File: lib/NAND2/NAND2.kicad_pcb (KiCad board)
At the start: 2 copper layers, 4 parts

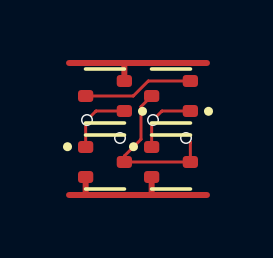
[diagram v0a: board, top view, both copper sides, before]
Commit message: Rename NAND into NAND2 and its inputs A and B into A1 and A2 (general convention when the pins can be swapped)
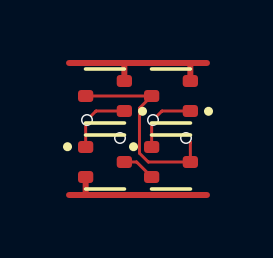
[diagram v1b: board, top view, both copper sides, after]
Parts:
- moved N1 2.20 mm to (1.10, 3.30), turned to 0 degrees
- moved N2 2.20 mm to (3.30, 3.30), turned to 0 degrees
- moved P1 2.20 mm to (1.10, 1.10), turned to 180 degrees
- moved P2 2.20 mm to (3.30, 1.10), turned to 180 degrees
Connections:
- net A renamed A1
- net B renamed A2
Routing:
- net int1: track 3.70 -> 1.12 mm
- net Y: track 5.64 -> 6.95 mm

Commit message: All cells now use 1mm*4mm grid rather than 1.1mm*4.4mm
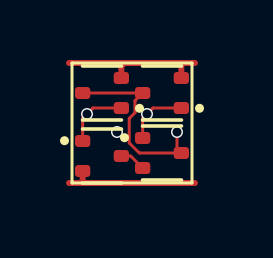
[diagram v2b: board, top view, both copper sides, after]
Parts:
- moved N2 0.42 mm to (3.00, 3.00)
- moved P2 0.32 mm to (3.00, 1.00)
- moved N1 0.22 mm to (1.00, 3.10)
- moved P1 0.14 mm to (1.00, 1.00)
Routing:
- net VDD: track 5.78 -> 5.25 mm
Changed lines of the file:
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@@
 	(footprint "Package_TO_SOT_SMD:SOT-523"
 		(layer "F.Cu")
-		(at 3.3 3.3)
+		(at 3 3)
 		(descr "SOT523, https://www.diodes.com/assets/Package-Files/SOT523.pdf")
 		(tags "SOT-523")
@@
 	(footprint "Package_TO_SOT_SMD:SOT-523"
 		(layer "F.Cu")
-		(at 3.3 1.1 180)
+		(at 3 1 180)
 		(descr "SOT523, https://www.diodes.com/assets/Package-Files/SOT523.pdf")
 		(tags "SOT-523")
@@
 	(footprint "Package_TO_SOT_SMD:SOT-523"
 		(layer "F.Cu")
-		(at 1.1 3.3)
+		(at 1 3.1)
 		(descr "SOT523, https://www.diodes.com/assets/Package-Files/SOT523.pdf")
 		(tags "SOT-523")
@@
 	(footprint "Package_TO_SOT_SMD:SOT-523"
 		(layer "F.Cu")
-		(at 1.1 1.1 180)
+		(at 1 1 180)
 		(descr "SOT523, https://www.diodes.com/assets/Package-Files/SOT523.pdf")
 		(tags "SOT-523")
@@
 		)
 	)
+	(gr_rect
+		(start 0 0)
+		(end 4 4)
+		(stroke
+			(width 0.1)
+			(type default)
+		)
+		(fill no)
+		(layer "F.SilkS")
+	)
 	(via
-		(at 1.6 2.5)
+		(at 1.5 2.3)
 		(size 0.4)
 		(drill 0.3)
@@
 	)
 	(segment
-		(start 2.542262 3.3)
-		(end 3.945 3.3)
+		(start 1.906738 2.664476)
+		(end 1.906738 1.851)
 		(width 0.1)
 		(layer "F.Cu")
@@
 	)
 	(segment
-		(start 2.655 1.1)
-		(end 2.249 1.506)
+		(start 2.355 1)
+		(end 0.355 1)
 		(width 0.1)
 		(layer "F.Cu")
@@
 	)
 	(segment
-		(start 2.249 3.006738)
-		(end 2.542262 3.3)
+		(start 2.099 1.658738)
+		(end 2.099 1.256)
 		(width 0.1)
 		(layer "F.Cu")
@@
 	)
 	(segment
-		(start 3.945 2.645)
-		(end 3.8 2.5)
+		(start 3.5 2.3)
+		(end 3.5 2.855)
 		(width 0.1)
 		(layer "F.Cu")
@@
 	)
 	(segment
-		(start 2.249 1.506)
-		(end 2.249 3.006738)
+		(start 3.645 3)
+		(end 2.242262 3)
 		(width 0.1)
 		(layer "F.Cu")
@@
 	)
 	(segment
-		(start 0.455 1.1)
-		(end 2.655 1.1)
+		(start 3.5 2.855)
+		(end 3.645 3)
 		(width 0.1)
 		(layer "F.Cu")
@@
 	)
 	(segment
-		(start 3.945 3.3)
-		(end 3.945 2.645)
+		(start 2.099 1.256)
+		(end 2.355 1)
 		(width 0.1)
 		(layer "F.Cu")
 		(net 1)
 	)
+	(segment
+		(start 1.906738 1.851)
+		(end 2.099 1.658738)
+		(width 0.1)
+		(layer "F.Cu")
+		(net 1)
+	)
+	(segment
+		(start 2.242262 3)
+		(end 1.906738 2.664476)
+		(width 0.1)
+		(layer "F.Cu")
+		(net 1)
+	)
 	(via
-		(at 3.8 2.5)
+		(at 3.5 2.3)
 		(size 0.4)
 		(drill 0.3)
@@
 	)
 	(segment
-		(start 0.45 4.4)
-		(end -0.1 4.4)
+		(start 0.355 3.5)
+		(end 0.355 3.945)
 		(width 0.2)
 		(layer "F.Cu")
@@
 	)
 	(segment
-		(start 4.5 4.4)
-		(end 0.45 4.4)
+		(start 0.45 4)
+		(end 0.3 4)
 		(width 0.2)
 		(layer "F.Cu")
@@
 	)
 	(segment
-		(start 0.455 4.395)
-		(end 0.45 4.4)
+		(start 4.1 4)
+		(end 0.45 4)
 		(width 0.2)
 		(layer "F.Cu")
@@
 	)
 	(segment
-		(start 0.455 3.8)
-		(end 0.455 4.395)
+		(start 0.355 3.945)
+		(end 0.3 4)
 		(width 0.2)
 		(layer "F.Cu")
@@
 	)
 	(segment
-		(start 0.8 1.6)
-		(end 0.5 1.9)
+		(start 0.455 4)
+		(end 0.45 4)
+		(width 0.2)
+		(layer "F.Cu")
+		(net 2)
+	)
+	(segment
+		(start 0.3 4)
+		(end -0.1 4)
+		(width 0.2)
+		(layer "F.Cu")
+		(net 2)
+	)
+	(segment
+		(start 0.5 1.7)
+		(end 0.7 1.5)
 		(width 0.1)
 		(layer "F.Cu")
@@
 	)
 	(segment
-		(start 0.455 2.8)
-		(end 0.455 1.945)
+		(start 0.355 2.6)
+		(end 0.355 1.845)
 		(width 0.1)
 		(layer "F.Cu")
@@
 	)
 	(segment
-		(start 0.455 1.945)
-		(end 0.5 1.9)
+		(start 0.355 1.845)
+		(end 0.5 1.7)
 		(width 0.1)
 		(layer "F.Cu")
@@
 	)
 	(segment
-		(start 1.745 1.6)
-		(end 0.8 1.6)
+		(start 0.7 1.5)
+		(end 1.645 1.5)
 		(width 0.1)
 		(layer "F.Cu")
@@
 	)
 	(via
-		(at 0.5 1.9)
+		(at 0.5 1.7)
 		(size 0.4)
 		(drill 0.3)
@@
 	)
 	(segment
-		(start 3.945 0.6)
-		(end 3.945 0.005)
+		(start 3.645 0.045)
+		(end 3.6 0)
 		(width 0.2)
 		(layer "F.Cu")
@@
 	)
 	(segment
-		(start 1.745 0.6)
-		(end 1.745 0.025)
+		(start 1.645 0.5)
+		(end 1.645 0.045)
+		(width 0.2)
+		(layer "F.Cu")
+		(net 4)
+	)
+	(segment
+		(start 1.645 0.045)
+		(end 1.6 0)
 		(width 0.2)
 		(layer "F.Cu")
@@
 	)
 	(segment
-		(start 4.5 0)
+		(start 3.6 0)
+		(end 1.6 0)
+		(width 0.2)
+		(layer "F.Cu")
+		(net 4)
+	)
+	(segment
+		(start 3.95 0)
+		(end 3.6 0)
+		(width 0.2)
+		(layer "F.Cu")
+		(net 4)
+	)
+	(segment
+		(start 3.645 0.5)
+		(end 3.645 0.045)
+		(width 0.2)
+		(layer "F.Cu")
+		(net 4)
+	)
+	(segment
+		(start 4.1 0)
 		(end 3.95 0)
 		(width 0.2)
@@
 	)
 	(segment
-		(start 3.95 0)
+		(start 1.6 0)
 		(end -0.1 0)
 		(width 0.2)
@@
 	)
 	(segment
-		(start 1.745 3.3)
-		(end 2.155 3.3)
+		(start 1.955 3.1)
+		(end 2.355 3.5)
 		(width 0.1)
 		(layer "F.Cu")
@@
 	)
 	(segment
-		(start 2.155 3.3)
-		(end 2.655 3.8)
+		(start 1.645 3)
+		(end 1.645 3.1)
 		(width 0.1)
 		(layer "F.Cu")
@@
 	)
 	(segment
-		(start 3 1.6)
-		(end 2.7 1.9)
+		(start 1.645 3.1)
+		(end 1.955 3.1)
+		(width 0.1)
+		(layer "F.Cu")
+		(net 5)
+	)
+	(segment
+		(start 2.7 1.5)
+		(end 3.645 1.5)
 		(width 0.1)
 		(layer "F.Cu")
@@
 	)
 	(segment
-		(start 3.945 1.6)
-		(end 3 1.6)
+		(start 2.5 1.7)
+		(end 2.7 1.5)
 		(width 0.1)
 		(layer "F.Cu")
@@
 	)
 	(segment
-		(start 2.655 2.8)
-		(end 2.655 1.945)
+		(start 2.355 2.5)
+		(end 2.355 1.845)
 		(width 0.1)
 		(layer "F.Cu")
@@
 	)
 	(segment
-		(start 2.655 1.945)
-		(end 2.7 1.9)
+		(start 2.355 1.845)
+		(end 2.5 1.7)
 		(width 0.1)
 		(layer "F.Cu")
@@
 	)
 	(via
-		(at 2.7 1.9)
+		(at 2.5 1.7)
 		(size 0.4)
 		(drill 0.3)

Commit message: Make the pads of my SOT523 footprint very slightly smaller, which is enough to route all the cells and leave the mosfets exactly on the grid
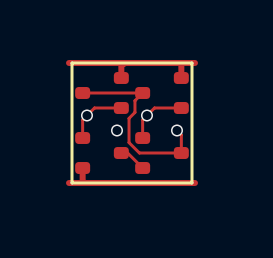
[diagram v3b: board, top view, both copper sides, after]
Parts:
- N1, N2, P1, P2: footprint Package_TO_SOT_SMD:SOT-523 -> RV523:SOT523
- moved N1 0.10 mm to (1.00, 3.00)

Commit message: Propagate MOSFET values to the cells' PCBs
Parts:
- N1, N2: value (none) -> NMOS
- P1, P2: value (none) -> PMOS
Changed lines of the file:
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@@
 			)
 		)
-		(property "Value" ""
+		(property "Value" "NMOS"
 			(at 0 0 0)
 			(layer "F.Fab")
@@
 			)
 		)
-		(property "Value" ""
+		(property "Value" "PMOS"
 			(at 0 0 180)
 			(layer "F.Fab")
@@
 			)
 		)
-		(property "Value" ""
+		(property "Value" "NMOS"
 			(at 0 0 0)
 			(layer "F.Fab")
@@
 			)
 		)
-		(property "Value" ""
+		(property "Value" "PMOS"
 			(at 0 0 180)
 			(layer "F.Fab")
